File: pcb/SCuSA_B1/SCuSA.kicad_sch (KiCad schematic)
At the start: 64 parts, among them J101 USB4135-GF-A, J102 JST_S2B-PH-SM4-x, J103 Binding_Post_PKI_10_A_Au, J104 Binding_Post_PKI_10_A_Au, J105 SMA_Straight_Jack_Female, J107 77311-118-02LF, J108 77311-118-02LF, Q101 DMN2041LSD, SW101 JS202011CQN, SW102 JS202011CQN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

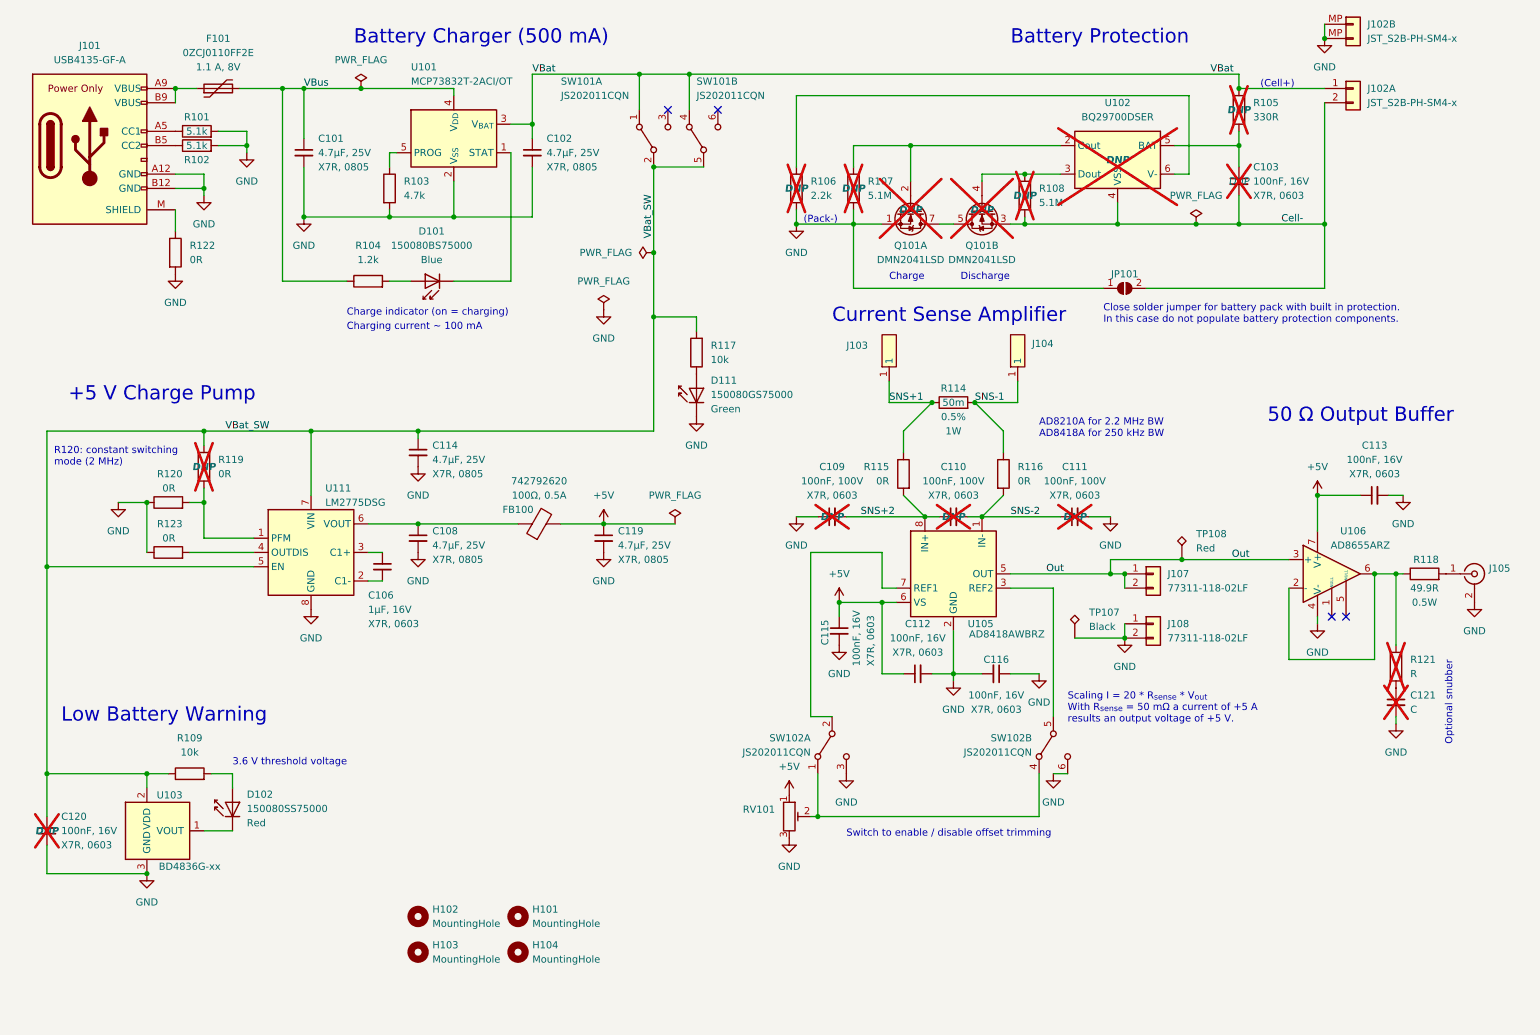
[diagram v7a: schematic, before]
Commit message: BOM modifications
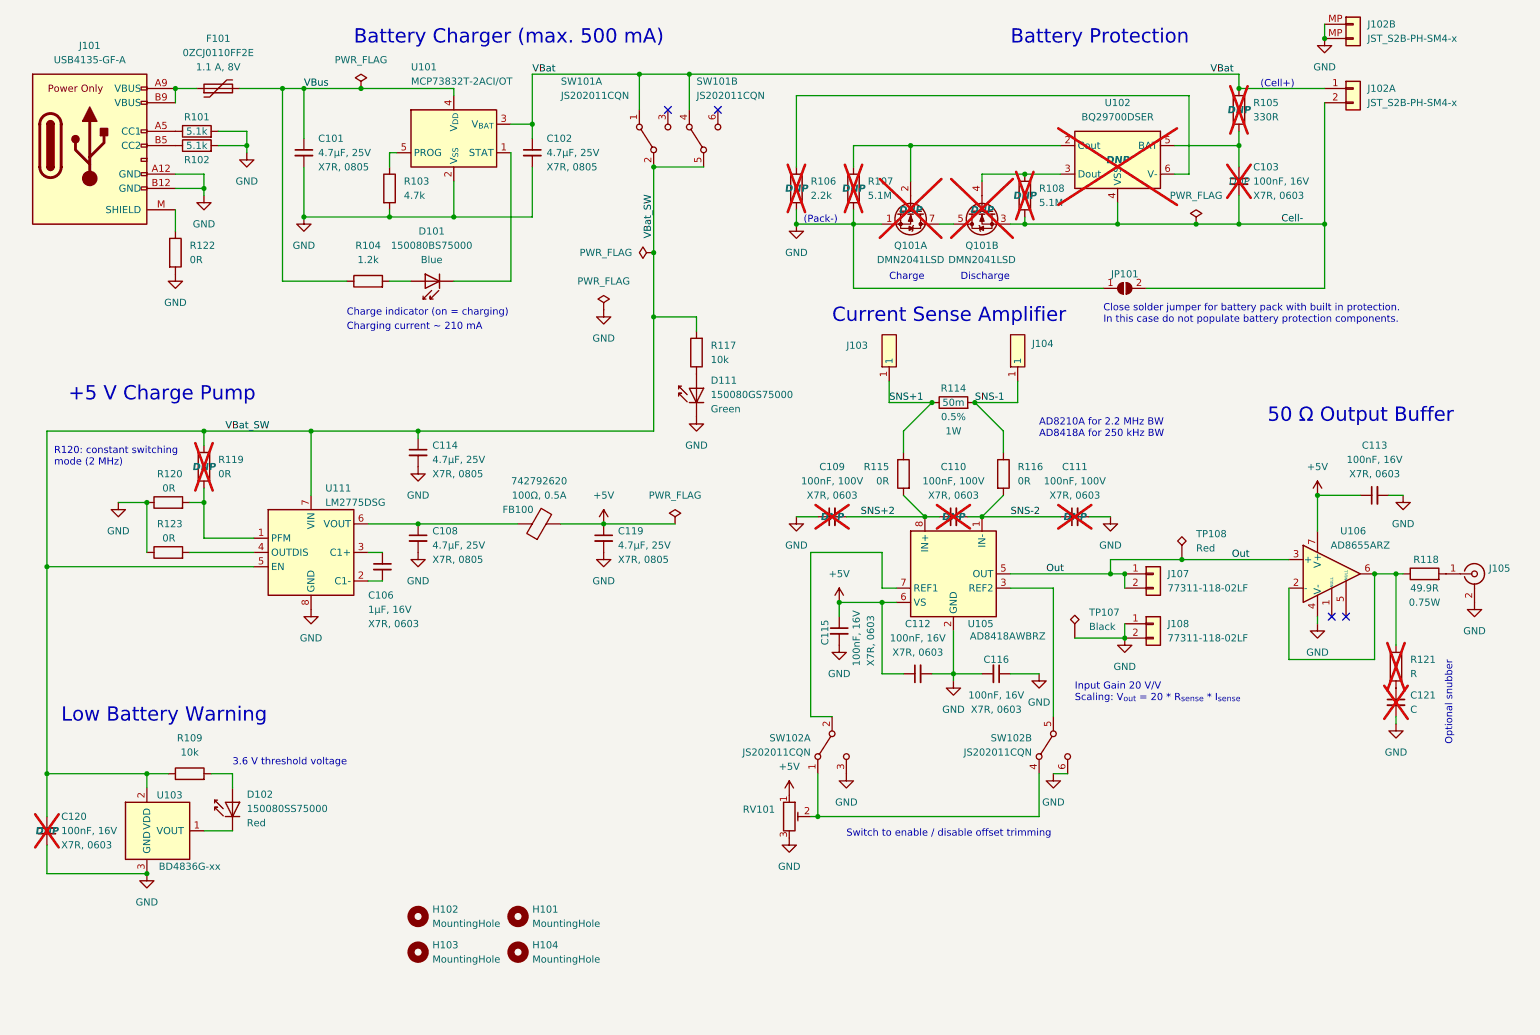
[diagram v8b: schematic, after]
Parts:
- R118: Power 0.5W -> 0.75W
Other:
- note added: "Battery Charger (max. 500 mA)"
- note added: "Charging current ~ 210 mA"
- note added: "Input Gain 20 V/V Scaling: V_{out} = 20 * R_{sense} * I_{sense}"
- note removed: "Battery Charger (500 mA)"
- note removed: "Charging current ~ 100 mA"
- note removed: "Scaling I = 20 * R_{sense} * V_{out} With R_{sense} = 50 mΩ a current of +5 A results an output voltage of +5 V."
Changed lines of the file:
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@@
     (effects (font (size 2.54 2.54)) (justify left bottom))
   )
-  (text "Charging current ~ 100 mA" (at 77.47 71.12 0)
+  (text "Charging current ~ 210 mA" (at 77.47 71.12 0)
     (effects (font (size 1.27 1.27)) (justify left bottom))
   )
@@
     (effects (font (size 1.27 1.27)) (justify left bottom))
   )
-  (text "Battery Charger (500 mA)" (at 78.74 20.32 0)
+  (text "Battery Charger (max. 500 mA)" (at 78.74 20.32 0)
     (effects (font (size 2.54 2.54)) (justify left bottom))
   )
@@
     (effects (font (size 2.54 2.54)) (justify left bottom))
   )
-  (text "Scaling I = 20 * R_{sense} * V_{out}\nWith R_{sense} = 50 mΩ a current of +5 A\nresults an output voltage of +5 V."
-    (at 205.74 140.97 0)
+  (text "Input Gain 20 V/V\nScaling: V_{out} = 20 * R_{sense} * I_{sense}"
+    (at 207.01 137.16 0)
     (effects (font (size 1.27 1.27)) (justify left bottom))
   )
@@
       (effects (font (size 1.27 1.27)) (justify left))
     )
-    (property "Value" "AD8418AWBRZ" (at 201.6598 125.0289 0)
+    (property "Value" "AD8418AWBRZ" (at 201.8179 125.3883 0)
       (effects (font (size 1.27 1.27)) (justify right))
     )
@@
       (effects (font (size 1.27 1.27)) hide)
     )
-    (property "Datasheet" "https://www.analog.com/media/en/technical-documentation/data-sheets/ad8410a.pdf" (at 201.93 132.08 0)
+    (property "Datasheet" "https://www.analog.com/media/en/technical-documentation/data-sheets/ad8418a.pdf" (at 201.93 132.08 0)
       (effects (font (size 1.27 1.27)) hide)
     )
@@
       (effects (font (size 1.27 1.27)) (justify left) hide)
     )
-    (property "Power" "0.5W" (at 269.24 119.38 90)
+    (property "Power" "0.75W" (at 269.24 119.38 90)
       (effects (font (size 1.27 1.27)))
     )
